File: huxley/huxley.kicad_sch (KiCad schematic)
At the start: 4 parts, among them J5 SMA_RF2-04A-T-00-50-G, U6 NVT2010PW_118

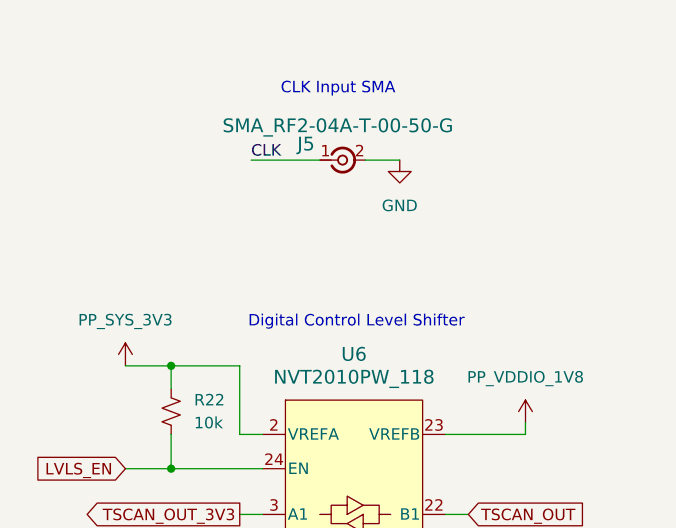
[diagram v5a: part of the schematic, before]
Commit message: fixed all bad refs; replaced analog discovery connector; change level shifter 3v3 to from analog discovery
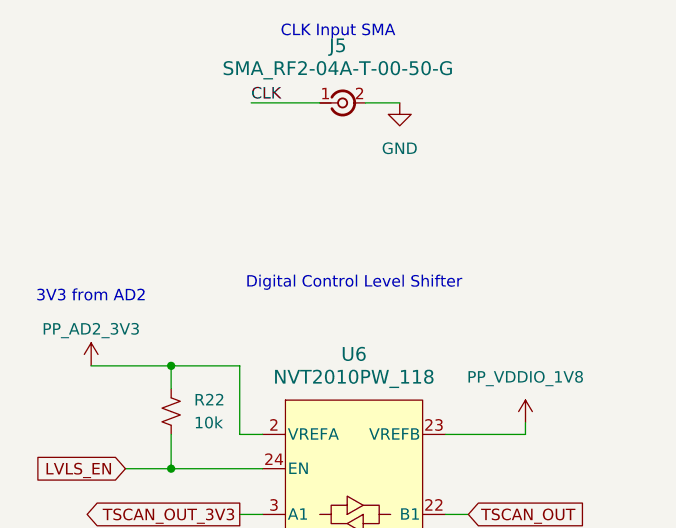
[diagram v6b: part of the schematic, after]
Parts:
- J5: footprint 726_footprints:CONN_RF2-04A-T-00-50-G_ADM -> 0_726_footprints:CONN_RF2-04A-T-00-50-G_ADM; symbol _PHASE:SMA_RF2-04A-T-00-50-G -> 0_PHASE:SMA_RF2-04A-T-00-50-G
- U6: footprint _726_Common:TSSOP24_SOT355-1_NXP -> 0_726_footprints:TSSOP24_SOT355-1_NXP; symbol _PHASE:NVT2010PW_118 -> 0_PHASE:NVT2010PW_118
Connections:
- net PP_SYS_3V3 renamed PP_AD2_3V3
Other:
- note added: "3V3 from AD2"
- moved on the sheet: J5
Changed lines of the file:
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@@
 	(wire
 		(pts
-			(xy 62.23 41.91) (xy 66.04 41.91)
+			(xy 62.23 35.56) (xy 66.04 35.56)
 		)
 		(stroke
@@
 	(wire
 		(pts
-			(xy 35.56 64.77) (xy 40.64 64.77)
+			(xy 31.75 64.77) (xy 40.64 64.77)
 		)
 		(stroke
@@
 	(wire
 		(pts
-			(xy 49.53 41.91) (xy 57.15 41.91)
+			(xy 49.53 35.56) (xy 57.15 35.56)
 		)
 		(stroke
@@
 	(text "CLK Input SMA\n"
 		(exclude_from_sim no)
-		(at 59.182 34.036 0)
+		(at 59.182 27.686 0)
+		(effects
+			(font
+				(size 1.27 1.27)
+			)
+		)
+	)
+	(text "3V3 from AD2"
+		(exclude_from_sim no)
+		(at 31.75 57.15 0)
 		(effects
 			(font
@@
 	(text "Digital Control Level Shifter"
 		(exclude_from_sim no)
-		(at 61.214 59.944 0)
+		(at 60.96 55.626 0)
 		(effects
 			(font
@@
 	)
 	(label "CLK"
-		(at 49.53 41.91 0)
+		(at 49.53 35.56 0)
 		(fields_autoplaced yes)
 		(effects
@@
 	(symbol
 		(lib_id "power:+1V2")
-		(at 35.56 64.77 0)
+		(at 31.75 64.77 0)
 		(unit 1)
 		(exclude_from_sim no)
@@
 		(dnp no)
 		(property "Reference" "#PWR025"
-			(at 35.56 68.58 0)
-			(effects
-				(font
-					(size 1.27 1.27)
-				)
-				(hide yes)
-			)
-		)
-		(property "Value" "PP_SYS_3V3"
-			(at 35.56 59.69 0)
+			(at 31.75 68.58 0)
+			(effects
+				(font
+					(size 1.27 1.27)
+				)
+				(hide yes)
+			)
+		)
+		(property "Value" "PP_AD2_3V3"
+			(at 31.75 60.706 0)
 			(effects
 				(font
@@
 		)
 		(property "Footprint" ""
-			(at 35.56 64.77 0)
+			(at 31.75 64.77 0)
 			(effects
 				(font
@@
 		)
 		(property "Datasheet" ""
-			(at 35.56 64.77 0)
+			(at 31.75 64.77 0)
 			(effects
 				(font
@@
 		)
 		(property "Description" "Power symbol creates a global label with name \"+1V2\""
-			(at 35.56 64.77 0)
+			(at 31.75 64.77 0)
 			(effects
 				(font
@@
 	(symbol
 		(lib_id "power:GND")
-		(at 66.04 41.91 0)
+		(at 66.04 35.56 0)
 		(unit 1)
 		(exclude_from_sim no)
@@
 		(fields_autoplaced yes)
 		(property "Reference" "#PWR016"
-			(at 66.04 48.26 0)
+			(at 66.04 41.91 0)
 			(effects
 				(font
@@
 		)
 		(property "Value" "GND"
-			(at 66.04 46.99 0)
+			(at 66.04 40.64 0)
 			(effects
 				(font
@@
 		)
 		(property "Footprint" ""
-			(at 66.04 41.91 0)
+			(at 66.04 35.56 0)
 			(effects
 				(font
@@
 		)
 		(property "Datasheet" ""
-			(at 66.04 41.91 0)
+			(at 66.04 35.56 0)
 			(effects
 				(font
@@
 		)
 		(property "Description" "Power symbol creates a global label with name \"GND\" , ground"
-			(at 66.04 41.91 0)
+			(at 66.04 35.56 0)
 			(effects
 				(font
@@
 	)
 	(symbol
-		(lib_id "_PHASE:SMA_RF2-04A-T-00-50-G")
-		(at 46.99 36.83 0)
+		(lib_id "0_PHASE:SMA_RF2-04A-T-00-50-G")
+		(at 46.99 30.48 0)
 		(unit 1)
 		(exclude_from_sim no)
@@
 		(fields_autoplaced yes)
 		(property "Reference" "J5"
-			(at 55.626 40.132 0)
+			(at 59.1704 29.21 0)
 			(effects
 				(font
@@
 		)
 		(property "Value" "SMA_RF2-04A-T-00-50-G"
-			(at 59.1704 38.1 0)
+			(at 59.1704 31.75 0)
 			(effects
 				(font
@@
 			)
 		)
-		(property "Footprint" "726_footprints:CONN_RF2-04A-T-00-50-G_ADM"
-			(at 46.99 36.83 0)
+		(property "Footprint" "0_726_footprints:CONN_RF2-04A-T-00-50-G_ADM"
+			(at 46.99 30.48 0)
 			(effects
 				(font
@@
 		)
 		(property "Datasheet" "112404"
-			(at 46.99 36.83 0)
+			(at 46.99 30.48 0)
 			(effects
 				(font
@@
 		)
 		(property "Description" ""
-			(at 46.99 36.83 0)
+			(at 46.99 30.48 0)
 			(effects
 				(font
@@
 	)
 	(symbol
-		(lib_id "_PHASE:NVT2010PW_118")
+		(lib_id "0_PHASE:NVT2010PW_118")
 		(at 60.96 96.52 0)
 		(unit 1)
@@
 			)
 		)
-		(property "Footprint" "_726_Common:TSSOP24_SOT355-1_NXP"
+		(property "Footprint" "0_726_footprints:TSSOP24_SOT355-1_NXP"
 			(at 29.464 122.428 0)
 			(effects

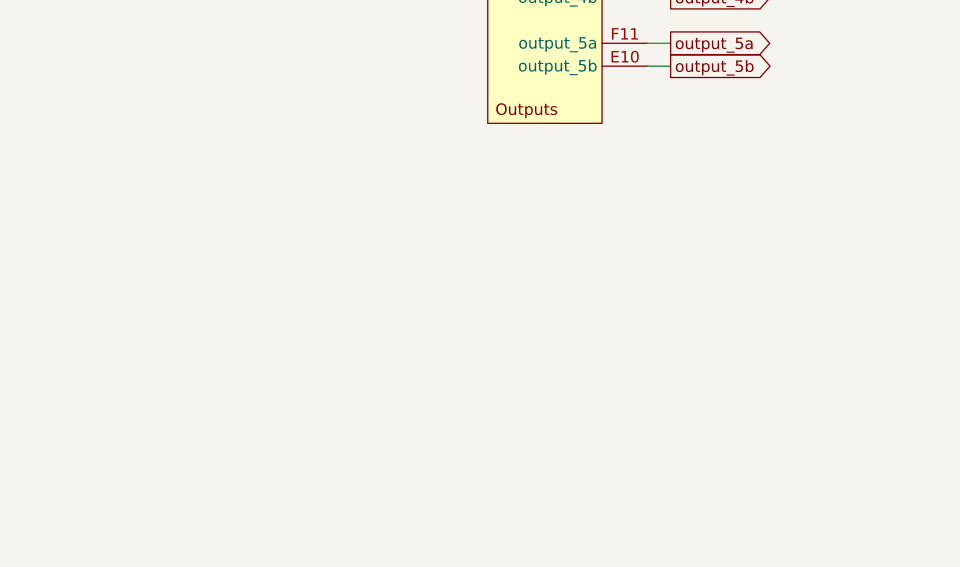
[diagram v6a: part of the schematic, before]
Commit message: minor schematic cleanup; addition of mounting holes; minor layout adjustment
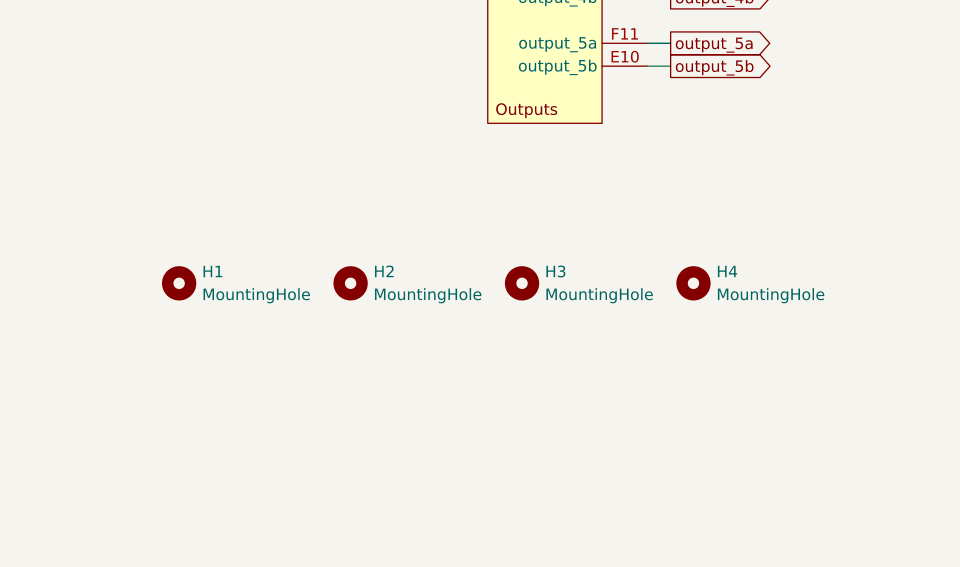
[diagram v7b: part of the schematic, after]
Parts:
- added H1, H2, H3, H4: MountingHole, MountingHole:MountingHole_3.2mm_M3_DIN965_Pad_TopBottom, symbol Mechanical:MountingHole

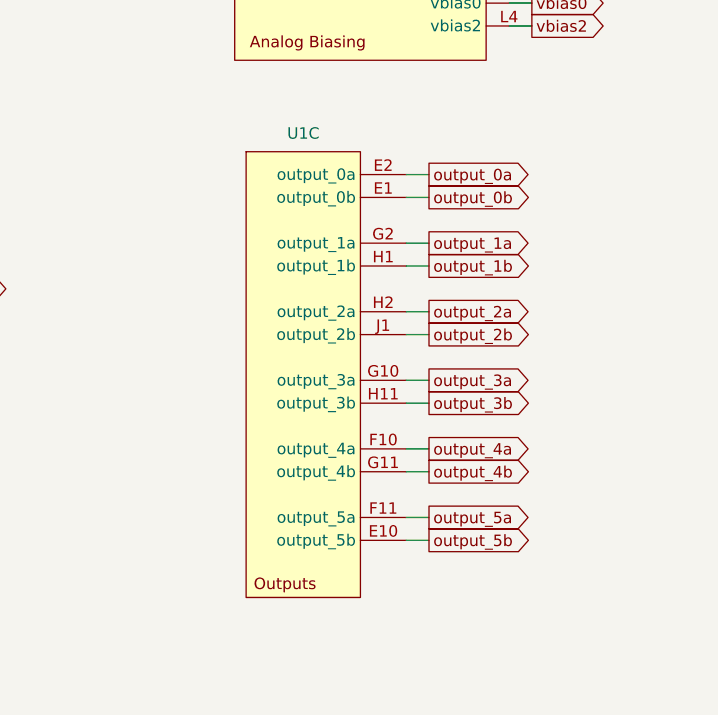
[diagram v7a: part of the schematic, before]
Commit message: changed output names to be kicad diffpair-style (+/-); board rearrangement wip
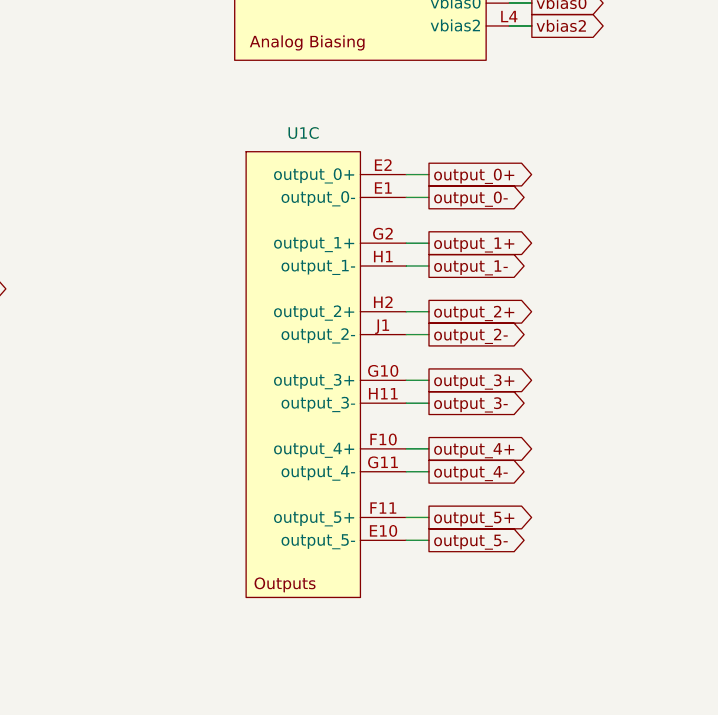
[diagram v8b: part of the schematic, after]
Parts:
- U1: footprint 0_726_footprints:CPG08462_Full -> _726_Common:CPG08462
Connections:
- net output_0a renamed output_0+
- net output_0b renamed output_0-
- net output_1a renamed output_1+
- net output_1b renamed output_1-
- net output_2a renamed output_2+
- net output_2b renamed output_2-
- net output_3a renamed output_3+
- net output_3b renamed output_3-
- net output_4a renamed output_4+
- net output_4b renamed output_4-
- net output_5a renamed output_5+
- net output_5b renamed output_5-
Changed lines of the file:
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@@
 		)
 	)
-	(global_label "output_2b"
+	(global_label "output_2-"
 		(shape output)
 		(at 232.41 90.17 0)
@@
 		)
 	)
-	(global_label "output_0b"
+	(global_label "output_0-"
 		(shape output)
 		(at 232.41 74.93 0)
@@
 		)
 	)
-	(global_label "output_5a"
+	(global_label "output_5+"
 		(shape output)
 		(at 232.41 110.49 0)
@@
 		)
 	)
-	(global_label "output_2a"
+	(global_label "output_2+"
 		(shape output)
 		(at 232.41 87.63 0)
@@
 		)
 	)
-	(global_label "output_0a"
+	(global_label "output_0+"
 		(shape output)
 		(at 232.41 72.39 0)
@@
 		)
 	)
-	(global_label "output_4a"
+	(global_label "output_4+"
 		(shape output)
 		(at 232.41 102.87 0)
@@
 		)
 	)
-	(global_label "output_1a"
+	(global_label "output_1+"
 		(shape output)
 		(at 232.41 80.01 0)
@@
 		)
 	)
-	(global_label "output_4b"
+	(global_label "output_4-"
 		(shape output)
 		(at 232.41 105.41 0)
@@
 		)
 	)
-	(global_label "output_5b"
+	(global_label "output_5-"
 		(shape output)
 		(at 232.41 113.03 0)
@@
 		)
 	)
-	(global_label "output_3a"
+	(global_label "output_3+"
 		(shape output)
 		(at 232.41 95.25 0)
@@
 		)
 	)
-	(global_label "output_3b"
+	(global_label "output_3-"
 		(shape output)
 		(at 232.41 97.79 0)
@@
 		)
 	)
-	(global_label "output_1b"
+	(global_label "output_1-"
 		(shape output)
 		(at 232.41 82.55 0)
@@
 	)
 	(symbol
+		(lib_name "PHASEIC_SOCKET_1")
 		(lib_id "0_PHASE:PHASEIC_SOCKET")
 		(at 218.44 76.2 0)
@@
 			)
 		)
-		(property "Footprint" "0_726_footprints:CPG08462_Full"
+		(property "Footprint" "_726_Common:CPG08462"
 			(at 218.44 67.31 0)
 			(effects
